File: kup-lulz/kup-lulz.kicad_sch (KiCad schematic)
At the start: 5 parts, among them M1 HEATSINK, M2 SCREWHOLE, M3 SCREWHOLE, M4 SCREWHOLE, M5 SCREWHOLE

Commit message: Continued initial work on kup-lulz devboard
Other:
- sheet FPGA support ports: added FPGA_DONE_3V3, FPGA_INIT_3V3, FPGA_RESET_N_3V3; removed none
- sheet Management ports: added 3V3, GND; removed none
- sheet QSFP28 interface ports: added none; removed QSFP28A_REFCLK0_N, QSFP28A_REFCLK0_P, QSFP28B_REFCLK0_N, QSFP28B_REFCLK0_P, QSFP28B_REFCLK1_N, QSFP28B_REFCLK1_P
- sheet SFP28 interfaces ports: added 3V3, GND, SFP0_MOD_ABS, SFP0_RX_LOS, SFP0_TX_FAULT, SFP1_I2C_SCL, SFP1_I2C_SDA, SFP1_MOD_ABS, SFP1_RS0, SFP1_RS1, SFP1_RX_LOS, SFP1_TX_DISABLE, SFP1_TX_FAULT, SFP28_REFCLK0_N, SFP28_REFCLK0_P, SFP2_I2C_SCL, SFP2_I2C_SDA, SFP2_MOD_ABS, SFP2_RS0, SFP2_RS1, SFP2_RX_LOS, SFP2_TX_DISABLE, SFP2_TX_FAULT, SFP3_I2C_SCL, SFP3_I2C_SDA, SFP3_MOD_ABS, SFP3_RS0, SFP3_RS1, SFP3_RX_LOS, SFP3_TX_DISABLE, SFP3_TX_FAULT; removed none
- sheet SMPM ports ports: added GND; removed none

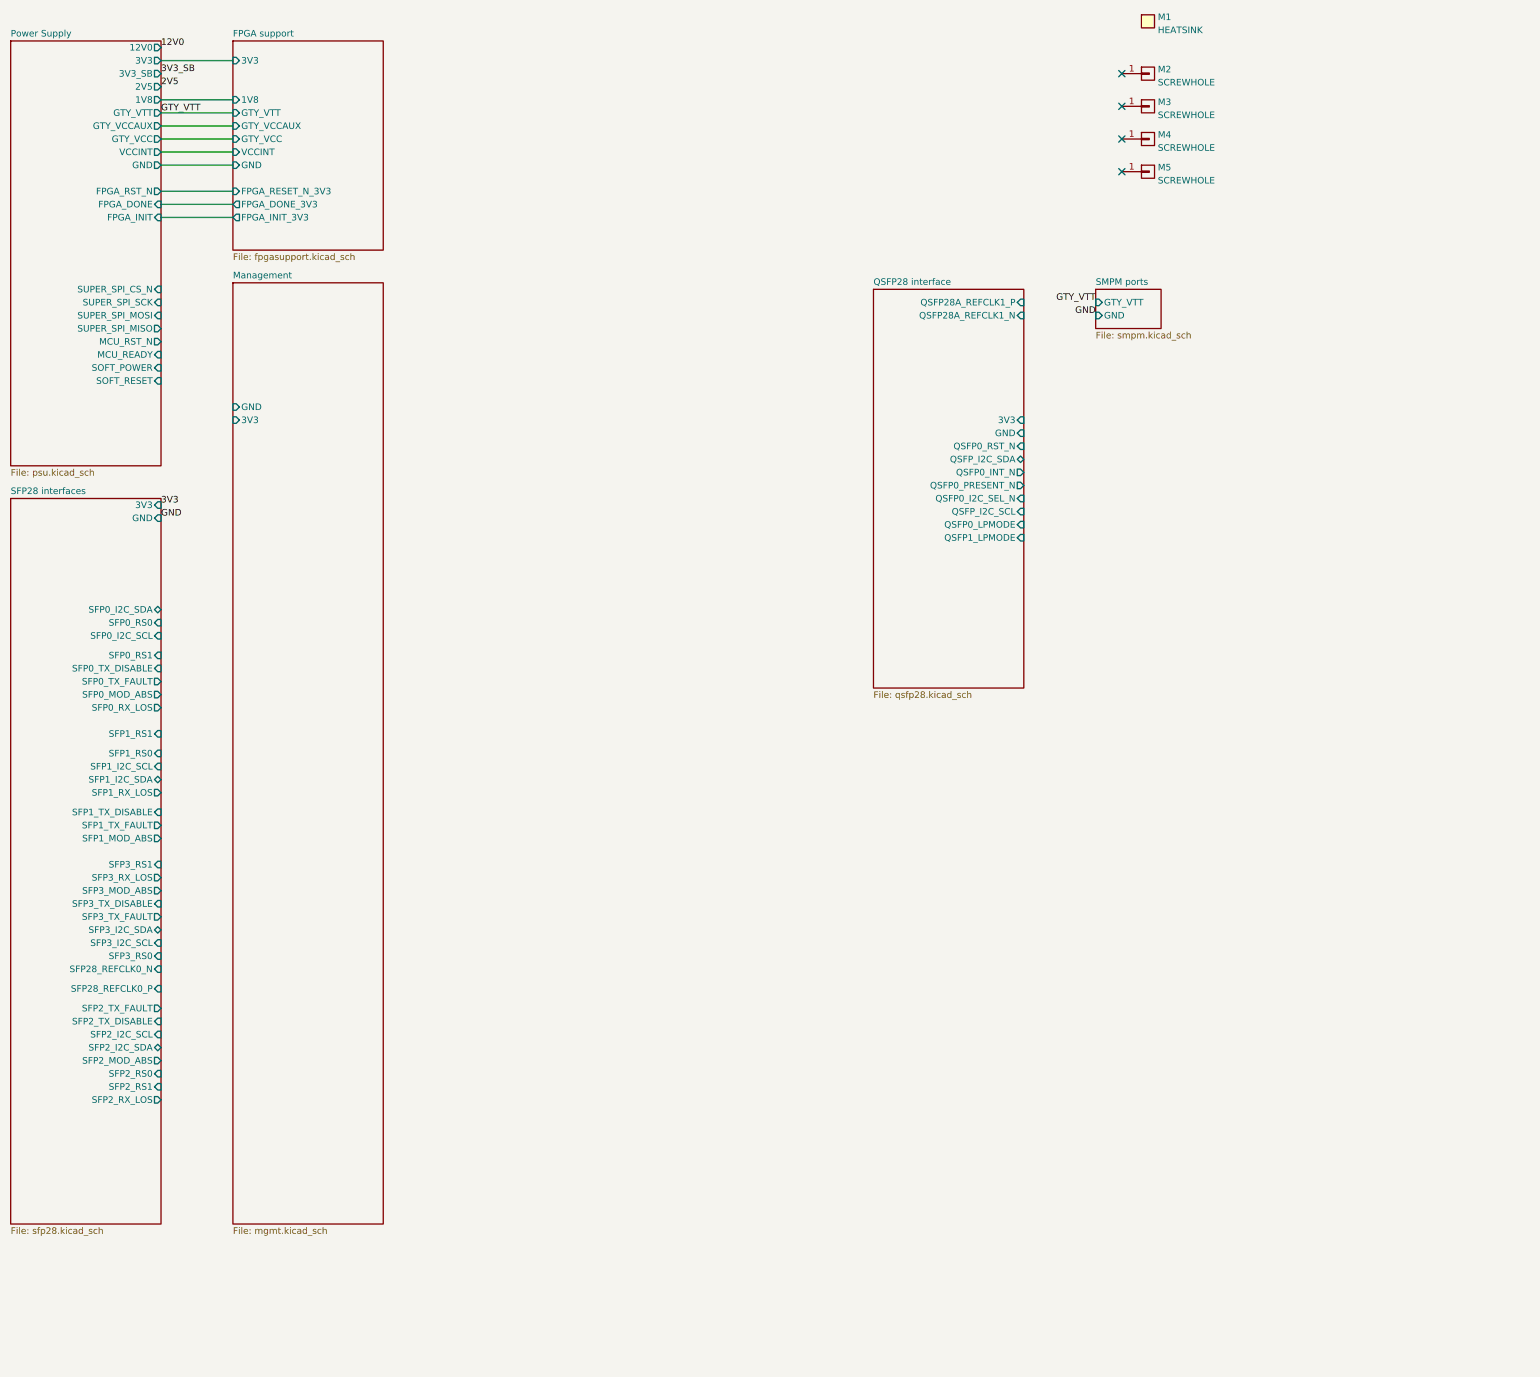
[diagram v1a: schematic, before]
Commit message: Continued initial layout of kup-lulz
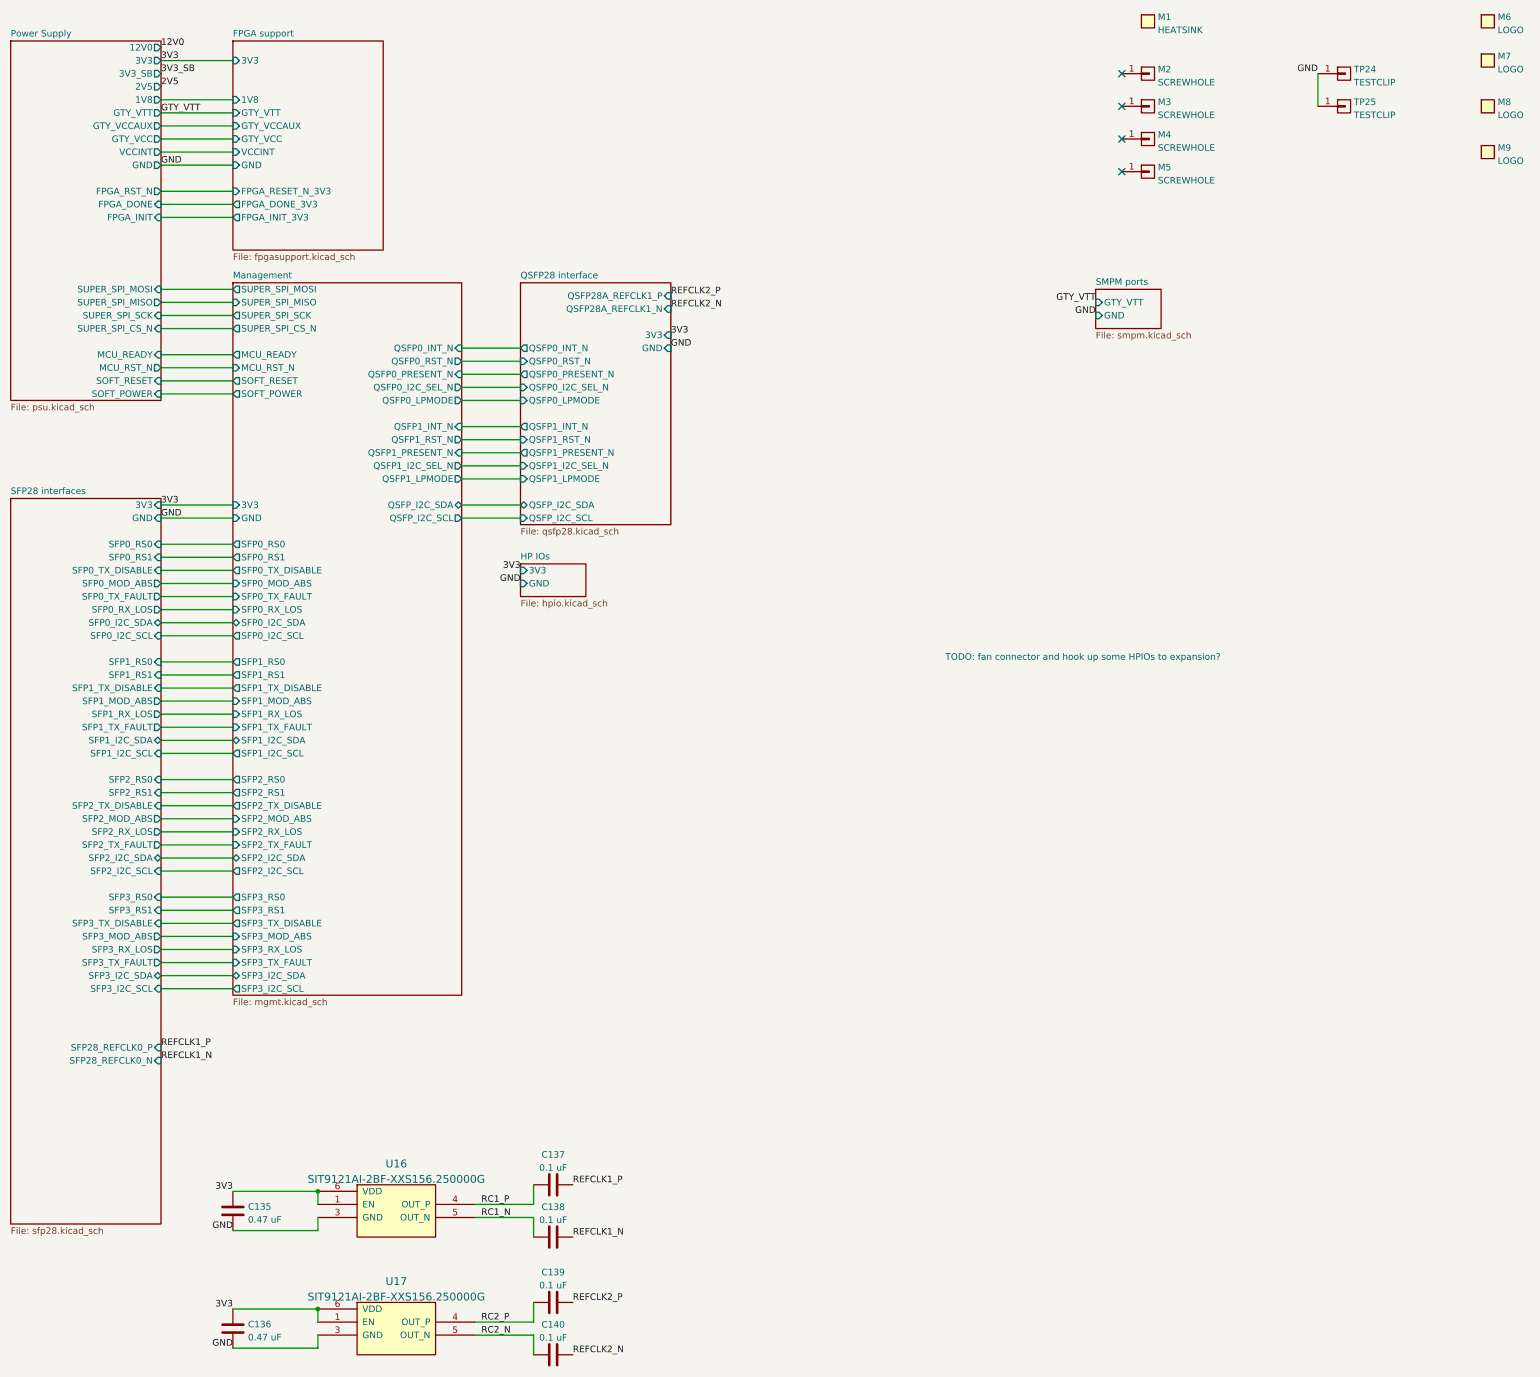
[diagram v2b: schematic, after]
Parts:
- added C135, C136: 0.47 uF, azonenberg_pcb:EIA_0402_CAP_NOSILK, symbol device:C
- added C137, C138, C139, C140: 0.1 uF, azonenberg_pcb:EIA_0402_CAP_NOSILK, symbol device:C
- added M6: LOGO, azonenberg_pcb:LONGTHING-1200DPI, symbol special-azonenberg:MECHANICAL
- added M7: LOGO, w_logo:Logo_silk_ROHS_5x2.8mm, symbol special-azonenberg:MECHANICAL
- added M8: LOGO, w_logo:Logo_silk_OSHW_6x6mm, symbol special-azonenberg:MECHANICAL
- added M9: LOGO, w_logo:Logo_silk_WEEE_3.4x5mm, symbol special-azonenberg:MECHANICAL
- added TP24, TP25: TESTCLIP, azonenberg_pcb:TESTPOINT_SMT_KEYSTONE_5016, symbol conn:CONN_01X01
- added U16, U17: SIT9121AI-2BF-XXS156.250000G, azonenberg_pcb:OSCILLATOR_LVDS_3.2x2.5, symbol osc-azonenberg:OSC_LVDS_NOPAD
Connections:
- net 3V3: now also C135.1, C136.1, U16.1 (EN), U16.6 (VDD), U17.1 (EN), U17.6 (VDD)
- net GND: now also C135.2, C136.2, TP24.1 (P1), TP25.1 (P1), U16.3 (GND), U17.3 (GND)
- new net RC1_N: C138.1, U16.5 (OUT_N)
- new net RC1_P: C137.1, U16.4 (OUT_P)
- new net RC2_N: C140.1, U17.5 (OUT_N)
- new net RC2_P: C139.1, U17.4 (OUT_P)
- new net REFCLK1_N: C138.2
- new net REFCLK1_P: C137.2
- new net REFCLK2_N: C140.2
- new net REFCLK2_P: C139.2
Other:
- added sheet HP IOs (hpio.kicad_sch)
- sheet Management ports: added MCU_READY, MCU_RST_N, QSFP0_I2C_SEL_N, QSFP0_INT_N, QSFP0_LPMODE, QSFP0_PRESENT_N, QSFP0_RST_N, QSFP1_I2C_SEL_N, QSFP1_INT_N, QSFP1_LPMODE, QSFP1_PRESENT_N, QSFP1_RST_N, QSFP_I2C_SCL, QSFP_I2C_SDA, SFP0_I2C_SCL, SFP0_I2C_SDA, SFP0_MOD_ABS, SFP0_RS0, SFP0_RS1, SFP0_RX_LOS, SFP0_TX_DISABLE, SFP0_TX_FAULT, SFP1_I2C_SCL, SFP1_I2C_SDA, SFP1_MOD_ABS, SFP1_RS0, SFP1_RS1, SFP1_RX_LOS, SFP1_TX_DISABLE, SFP1_TX_FAULT, SFP2_I2C_SCL, SFP2_I2C_SDA, SFP2_MOD_ABS, SFP2_RS0, SFP2_RS1, SFP2_RX_LOS, SFP2_TX_DISABLE, SFP2_TX_FAULT, SFP3_I2C_SCL, SFP3_I2C_SDA, SFP3_MOD_ABS, SFP3_RS0, SFP3_RS1, SFP3_RX_LOS, SFP3_TX_DISABLE, SFP3_TX_FAULT, SOFT_POWER, SOFT_RESET, SUPER_SPI_CS_N, SUPER_SPI_MISO, SUPER_SPI_MOSI, SUPER_SPI_SCK; removed none
- sheet QSFP28 interface ports: added QSFP1_I2C_SEL_N, QSFP1_INT_N, QSFP1_PRESENT_N, QSFP1_RST_N; removed none
- note added: "TODO: fan connector and hook up some HPIOs to expansion?"
- company: (none) -> Antikernel Labs

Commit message: Continued initial layout
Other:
- sheet Power Supply ports: added none; removed 2V5
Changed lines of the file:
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@@
-    (effects (font (size 1.27 1.27)) (justify left bottom))
-  )
-  (label "2V5" (at 53.34 31.75 0)
     (effects (font (size 1.27 1.27)) (justify left bottom))
   )
@@
     )
     (pin "3V3" output (at 53.34 26.67 0)
-      (effects (font (size 1.27 1.27)) (justify right))
-    )
-    (pin "2V5" output (at 53.34 31.75 0)
       (effects (font (size 1.27 1.27)) (justify right))
     )
@@
       (reference "C13") (unit 1) (value "22 uF 25V") (footprint "azonenberg_pcb:EIA_1812_CAP_NOSILK")
     )
-    (path "/141d8977-f4d9-41b5-a51c-3451b2afc8fb/37d2f7f4-6ee1-47b8-97e9-0015b531372a"
-      (reference "C14") (unit 1) (value "22 uF 25V") (footprint "azonenberg_pcb:EIA_1812_CAP_NOSILK")
-    )
     (path "/141d8977-f4d9-41b5-a51c-3451b2afc8fb/d552f331-d0fd-4ed7-bb88-35bddd28bfd2"
       (reference "C15") (unit 1) (value "22 uF 25V") (footprint "azonenberg_pcb:EIA_1812_CAP_NOSILK")
@@
       (reference "C17") (unit 1) (value "22 uF 25V") (footprint "azonenberg_pcb:EIA_1812_CAP_NOSILK")
     )
-    (path "/141d8977-f4d9-41b5-a51c-3451b2afc8fb/0e66f14f-a86b-461c-a605-620f90bd39a1"
-      (reference "C18") (unit 1) (value "22 uF 25V") (footprint "azonenberg_pcb:EIA_1812_CAP_NOSILK")
-    )
     (path "/141d8977-f4d9-41b5-a51c-3451b2afc8fb/2aa2d5b4-1fe2-4eb8-ad9d-adb5fea0c5d3"
       (reference "C19") (unit 1) (value "22 uF 25V") (footprint "azonenberg_pcb:EIA_1812_CAP_NOSILK")
@@
       (reference "C27") (unit 1) (value "220 uF") (footprint "azonenberg_pcb:EIA_1210_CAP_NOSILK")
     )
-    (path "/141d8977-f4d9-41b5-a51c-3451b2afc8fb/ea4dc580-538a-4bc6-986e-135c1d469498"
-      (reference "C28") (unit 1) (value "220 uF") (footprint "azonenberg_pcb:EIA_1210_CAP_NOSILK")
-    )
     (path "/141d8977-f4d9-41b5-a51c-3451b2afc8fb/287209ae-2a1c-4f32-8f0b-565abce1a9ce"
       (reference "C29") (unit 1) (value "220 uF") (footprint "azonenberg_pcb:EIA_1210_CAP_NOSILK")
@@
       (reference "C31") (unit 1) (value "220 uF") (footprint "azonenberg_pcb:EIA_1210_CAP_NOSILK")
     )
-    (path "/141d8977-f4d9-41b5-a51c-3451b2afc8fb/6977e53f-3882-4a84-83b4-a8f6be830409"
-      (reference "C32") (unit 1) (value "220 uF") (footprint "azonenberg_pcb:EIA_1210_CAP_NOSILK")
-    )
     (path "/141d8977-f4d9-41b5-a51c-3451b2afc8fb/df7c352c-c798-4479-bdf8-ba302bbb1419"
       (reference "C33") (unit 1) (value "220 uF") (footprint "azonenberg_pcb:EIA_1210_CAP_NOSILK")
@@
       (reference "C35") (unit 1) (value "DNP") (footprint "azonenberg_pcb:EIA_1210_CAP_NOSILK")
     )
-    (path "/141d8977-f4d9-41b5-a51c-3451b2afc8fb/1eac4326-6875-4832-b39b-e74d8f05a475"
-      (reference "C36") (unit 1) (value "DNP") (footprint "azonenberg_pcb:EIA_1210_CAP_NOSILK")
-    )
     (path "/141d8977-f4d9-41b5-a51c-3451b2afc8fb/a21a66c4-c4bb-4d8d-8468-5f9c241615c9"
       (reference "C37") (unit 1) (value "DNP") (footprint "azonenberg_pcb:EIA_1210_CAP_NOSILK")
@@
       (reference "R17") (unit 1) (value "4.7k") (footprint "azonenberg_pcb:EIA_0402_RES_NOSILK")
     )
-    (path "/141d8977-f4d9-41b5-a51c-3451b2afc8fb/2e14ac19-1560-436a-aeaf-210d7edee7d2"
-      (reference "R18") (unit 1) (value "3k") (footprint "azonenberg_pcb:EIA_0402_RES_NOSILK")
-    )
     (path "/141d8977-f4d9-41b5-a51c-3451b2afc8fb/0a4c9555-36a9-44e8-9915-3957b04a095d"
       (reference "R19") (unit 1) (value "20k") (footprint "azonenberg_pcb:EIA_0402_RES_NOSILK")
@@
       (reference "R21") (unit 1) (value "300") (footprint "azonenberg_pcb:EIA_0402_RES_NOSILK")
     )
-    (path "/141d8977-f4d9-41b5-a51c-3451b2afc8fb/8600f8c9-f078-4da5-963a-2c5cb804a716"
-      (reference "R22") (unit 1) (value "160") (footprint "azonenberg_pcb:EIA_0402_RES_NOSILK")
-    )
     (path "/141d8977-f4d9-41b5-a51c-3451b2afc8fb/17e0b673-b505-4424-968a-cf62fb68e343"
       (reference "R23") (unit 1) (value "0") (footprint "azonenberg_pcb:EIA_0402_RES_NOSILK")
@@
       (reference "R35") (unit 1) (value "1K") (footprint "azonenberg_pcb:EIA_0402_RES_NOSILK")
     )
-    (path "/141d8977-f4d9-41b5-a51c-3451b2afc8fb/677f46dd-7046-4b9c-acad-09fc807477ce"
-      (reference "R36") (unit 1) (value "10K") (footprint "azonenberg_pcb:EIA_0402_RES_NOSILK")
-    )
-    (path "/141d8977-f4d9-41b5-a51c-3451b2afc8fb/b9dd5aa5-d29e-495d-a8bd-4e426f9d80ad"
-      (reference "R37") (unit 1) (value "1K") (footprint "azonenberg_pcb:EIA_0402_RES_NOSILK")
-    )
     (path "/141d8977-f4d9-41b5-a51c-3451b2afc8fb/a783064d-0129-4d9e-bcc9-97219b403234"
       (reference "R38") (unit 1) (value "10K") (footprint "azonenberg_pcb:EIA_0402_RES_NOSILK")
@@
       (reference "R57") (unit 1) (value "4.7K") (footprint "azonenberg_pcb:EIA_0402_RES_NOSILK")
     )
-    (path "/4620982e-4f83-4fcb-97c5-c21ab596d66b/e78fc051-0b40-4a83-8515-eb8de9cdf6fb"
-      (reference "R58") (unit 1) (value "4.7K") (footprint "azonenberg_pcb:EIA_0402_RES_NOSILK")
-    )
-    (path "/4620982e-4f83-4fcb-97c5-c21ab596d66b/85e69340-875a-4b8e-ae5b-d9c076d057f1"
-      (reference "R59") (unit 1) (value "4.7K") (footprint "azonenberg_pcb:EIA_0402_RES_NOSILK")
-    )
     (path "/8853104e-72eb-4ea7-9d5b-06a6795b0525/d5208e00-5d4e-4f38-906d-869d3e1bfef1"
       (reference "R60") (unit 1) (value "1K") (footprint "azonenberg_pcb:EIA_0402_RES_NOSILK")
@@
       (reference "TP4") (unit 1) (value "TESTPOINT") (footprint "azonenberg_pcb:TESTPOINT_SMT_0.5MM")
     )
-    (path "/141d8977-f4d9-41b5-a51c-3451b2afc8fb/e4d73bd1-eec0-418d-b3f6-f591ee6ff609"
-      (reference "TP5") (unit 1) (value "TESTPOINT") (footprint "azonenberg_pcb:TESTPOINT_SMT_0.5MM")
-    )
     (path "/141d8977-f4d9-41b5-a51c-3451b2afc8fb/d4723641-02b5-49c9-aa41-1103287d3e6b"
       (reference "TP6") (unit 1) (value "TESTPOINT") (footprint "azonenberg_pcb:TESTPOINT_SMT_0.5MM")
@@
       (reference "TP16") (unit 1) (value "U.FL") (footprint "azonenberg_pcb:CONN_U.FL_TE_1909763-1")
     )
-    (path "/141d8977-f4d9-41b5-a51c-3451b2afc8fb/6059c3ed-68f0-4672-a619-1e3108363d56"
-      (reference "TP17") (unit 1) (value "U.FL") (footprint "azonenberg_pcb:CONN_U.FL_TE_1909763-1")
-    )
     (path "/a85f8a39-3bba-49df-9845-885441be9553/0ef537b8-d7c7-4188-9dd1-2a998bdad157"
       (reference "TP18") (unit 1) (value "U.FL") (footprint "azonenberg_pcb:CONN_U.FL_TE_1909763-1")
@@
       (reference "U5") (unit 1) (value "MYMGK00504ERSR") (footprint "azonenberg_pcb:MODULE_MURATA_MYMGK00504ERSR")
     )
-    (path "/141d8977-f4d9-41b5-a51c-3451b2afc8fb/fef93a48-6175-4c63-a4bf-6c2c453c77ba"
-      (reference "U6") (unit 1) (value "MYMGK00504ERSR") (footprint "azonenberg_pcb:MODULE_MURATA_MYMGK00504ERSR")
-    )
     (path "/141d8977-f4d9-41b5-a51c-3451b2afc8fb/f6e695fa-1b73-4220-a562-d3afad07075a"

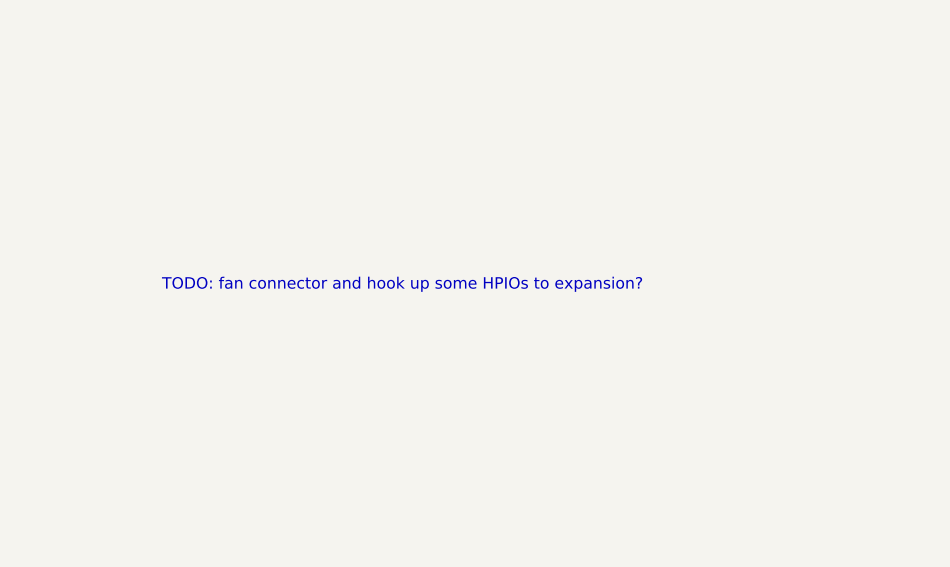
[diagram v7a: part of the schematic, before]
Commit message: Fully routed and DRC clean, added stitching vias on 5mm grid. Still needs layer-change vias for diffpairs and connector launch optimization
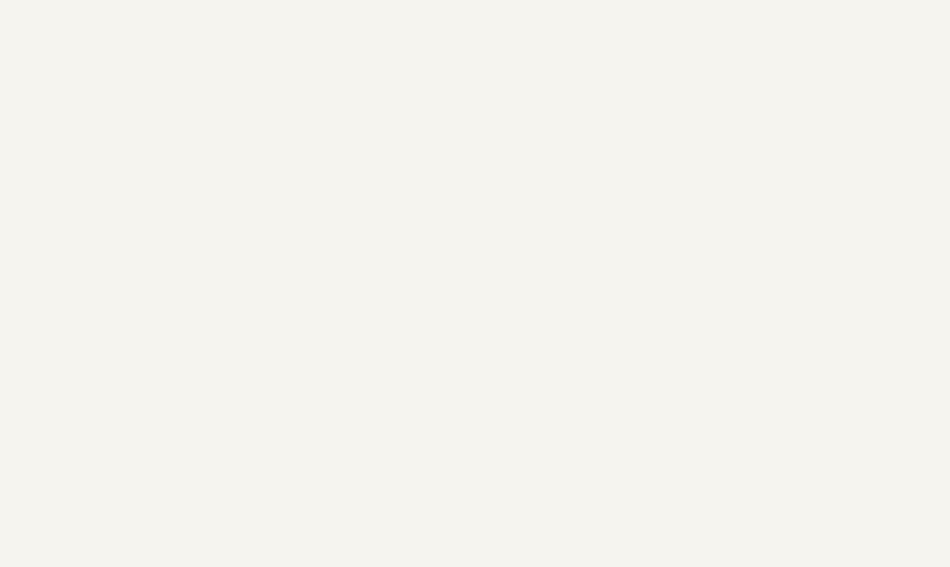
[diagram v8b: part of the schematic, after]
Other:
- note removed: "TODO: fan connector and hook up some HPIOs to expansion?"
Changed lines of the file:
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@@
     (stroke (width 0) (type default) (color 0 0 0 0))
-  )
-  (text "TODO: fan connector and hook up some HPIOs to expansion?"
-    (at 205.74 143.51 0)
-    (effects (font (size 1.27 1.27)) (justify left bottom))
   )
   (label "REFCLK2_P" (at 133.35 267.97 0)
@@
       (reference "C13") (unit 1) (value "22 uF 25V") (footprint "azonenberg_pcb:EIA_1812_CAP_NOSILK")
     )
+    (path "/141d8977-f4d9-41b5-a51c-3451b2afc8fb/5f20e7ac-94f4-43d8-a294-f090c6c55771"
+      (reference "C14") (unit 1) (value "10 uF 25V") (footprint "azonenberg_pcb:EIA_1210_CAP_NOSILK")
+    )
     (path "/141d8977-f4d9-41b5-a51c-3451b2afc8fb/d552f331-d0fd-4ed7-bb88-35bddd28bfd2"
       (reference "C15") (unit 1) (value "22 uF 25V") (footprint "azonenberg_pcb:EIA_1812_CAP_NOSILK")
@@
       (reference "D2") (unit 1) (value "RED") (footprint "azonenberg_pcb:EIA_0603_LED")
     )
+    (path "/141d8977-f4d9-41b5-a51c-3451b2afc8fb/bdfa2acb-ad77-48cf-95ba-a072a90b7d3e"
+      (reference "D3") (unit 1) (value "SZESD7471N2T5G") (footprint "azonenberg_pcb:SOD882")
+    )
+    (path "/141d8977-f4d9-41b5-a51c-3451b2afc8fb/d212e6db-8ad4-47bc-8b1e-1f496a7396ed"
+      (reference "D4") (unit 1) (value "SZESD7471N2T5G") (footprint "azonenberg_pcb:SOD882")
+    )
     (path "/141d8977-f4d9-41b5-a51c-3451b2afc8fb/6f041a72-539b-4789-a99d-c8d166db74dd"
       (reference "F1") (unit 1) (value "2A") (footprint "azonenberg_pcb:EIA_0603_CAP_NOSILK")
@@
       (reference "J12") (unit 1) (value "SFP_CAGE") (footprint "azonenberg_pcb:CONN_SFP_CAGE_TE_2007194-1")
     )
+    (path "/141d8977-f4d9-41b5-a51c-3451b2afc8fb/af6c5525-63a9-4866-b43b-d6746aaaed5b"
+      (reference "J13") (unit 1) (value "FAN_01") (footprint "azonenberg_pcb:CONN_MOLEX_KK_0470531000")
+    )
     (path "/a85f8a39-3bba-49df-9845-885441be9553/2c7c4d4f-c2d4-4d56-aa03-e7f27d7e76ea"
       (reference "J15") (unit 1) (value "CONN_QSFP_HOST") (footprint "azonenberg_pcb:CONN_ZQSFP+_TE_1551920-2")
@@
       (reference "R17") (unit 1) (value "4.7k") (footprint "azonenberg_pcb:EIA_0402_RES_NOSILK")
     )
+    (path "/141d8977-f4d9-41b5-a51c-3451b2afc8fb/95845f29-396e-472c-8056-7f13b28d2c28"
+      (reference "R18") (unit 1) (value "10K") (footprint "azonenberg_pcb:EIA_0402_RES_NOSILK")
+    )
     (path "/141d8977-f4d9-41b5-a51c-3451b2afc8fb/0a4c9555-36a9-44e8-9915-3957b04a095d"
